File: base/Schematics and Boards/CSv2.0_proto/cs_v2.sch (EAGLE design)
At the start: 80 parts, among them J101 J-JTAG-CORTEX-NEEDLE6LEGS, J301 HIROSE-DF40_44-PIN_CONNECTORS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, J302 HIROSE-DF40_30-PIN_CONNECTORS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, Q201 FK3303010L, Q202 DMG3415UFY4Q-7, Q203 FK3303010L, Q204 FK3303010L, U101 ATSAMD51, U102 AT25SF641-MHB-T, U201 COULOMB-MAX17262, U202 MAX77827BEWC+T, U203 SENSOR-SI7006, U204 LOADSWITCH-MIC94164, U205 LOADSWITCH-MIC94164, Y101 16M, Y102 ABS07-32.768KHZ-9-T

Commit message: Avoided catastrophe from file inconsistencies
Several hours of nightmare-inducing file-fiddling later...
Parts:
- J101: value J-JTAG-CORTEX-NEEDLE6LEGS -> J-JTAG-CORTEX-NEEDLE6-LEGS; device Connectors:J-JTAG-CORTEX-NEEDLE6LEGS -> Connectors:J-JTAG-CORTEX-NEEDLE6-LEGS
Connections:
- removed net N$1: S201.O
- net CC_IN: no longer S201.O
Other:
- moved on the sheet: C201, C203, U201
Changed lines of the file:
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@@
 <part name="JP205" library="Connectors" deviceset="JUMPER-SMT_2_NC_PASTE" device="_NO-SILK" package3d_urn="urn:adsk.eagle:package:39283/1"/>
 <part name="JP204" library="Connectors" deviceset="JUMPER-SMT_2_NC_PASTE" device="_NO-SILK" package3d_urn="urn:adsk.eagle:package:39283/1"/>
-<part name="J101" library="Connectors" deviceset="J-JTAG-CORTEX-NEEDLE6" device="LEGS"/>
+<part name="J101" library="Connectors" deviceset="J-JTAG-CORTEX-NEEDLE6" device="-LEGS"/>
 <part name="R106" library="Resistors" deviceset="R-" device="0402" value="1k">
 <attribute name="PART_NO" value="ERJ-2GEJ102X"/>
@@
 </segment>
 </net>
-<net name="N$1" class="0">
-<segment>
-<pinref part="S201" gate="1" pin="O"/>
-<wire x1="104.14" y1="177.8" x2="109.22" y2="177.8" width="0.1524" layer="91"/>
-</segment>
-</net>
 </nets>
 </sheet>
@@
 should be placed near XTALs</text>
 <text x="121.92" y="193.04" size="3.81" layer="91">Current Monitor</text>
-<text x="165.1" y="182.88" size="1.778" layer="91">Do we lose info about battery
+<text x="165.1" y="177.8" size="1.778" layer="91">Do we lose info about battery
 by not having the input directly
 connected to the battery?</text>
@@
 <attribute name="PART_NO" x="99.06" y="175.26" size="1.778" layer="96" display="off"/>
 </instance>
-<instance part="U201" gate="G$1" x="137.16" y="172.72" smashed="yes">
-<attribute name="NAME" x="127" y="185.42" size="1.778" layer="95"/>
-<attribute name="MP" x="137.16" y="172.72" size="1.778" layer="96" display="off"/>
-<attribute name="PART_NO" x="137.16" y="172.72" size="1.778" layer="96" display="off"/>
-</instance>
-<instance part="C201" gate="G$1" x="111.76" y="172.72" smashed="yes">
-<attribute name="NAME" x="112.776" y="173.355" size="1.778" layer="95"/>
-<attribute name="VALUE" x="112.776" y="168.529" size="1.778" layer="96"/>
-<attribute name="MP" x="111.76" y="172.72" size="1.778" layer="96" display="off"/>
-<attribute name="PART_NO" x="111.76" y="172.72" size="1.778" layer="96" display="off"/>
-</instance>
-<instance part="C203" gate="G$1" x="154.94" y="157.48" smashed="yes">
-<attribute name="NAME" x="155.956" y="158.115" size="1.778" layer="95"/>
-<attribute name="VALUE" x="155.956" y="153.289" size="1.778" layer="96"/>
-<attribute name="MP" x="154.94" y="157.48" size="1.778" layer="96" display="off"/>
-<attribute name="PART_NO" x="154.94" y="157.48" size="1.778" layer="96" display="off"/>
-</instance>
-<instance part="GND217" gate="1" x="154.94" y="147.32" smashed="yes">
-<attribute name="VALUE" x="147.193" y="146.685" size="1.778" layer="96"/>
-</instance>
-<instance part="GND211" gate="1" x="111.76" y="162.56" smashed="yes">
-<attribute name="VALUE" x="109.093" y="159.385" size="1.778" layer="96"/>
-</instance>
-<instance part="GND214" gate="1" x="137.16" y="152.4" smashed="yes">
-<attribute name="VALUE" x="134.493" y="149.225" size="1.778" layer="96"/>
+<instance part="U201" gate="G$1" x="137.16" y="167.64" smashed="yes">
+<attribute name="NAME" x="127" y="180.34" size="1.778" layer="95"/>
+<attribute name="MP" x="137.16" y="167.64" size="1.778" layer="96" display="off"/>
+<attribute name="PART_NO" x="137.16" y="167.64" size="1.778" layer="96" display="off"/>
+</instance>
+<instance part="C201" gate="G$1" x="111.76" y="167.64" smashed="yes">
+<attribute name="NAME" x="112.776" y="168.275" size="1.778" layer="95"/>
+<attribute name="VALUE" x="112.776" y="163.449" size="1.778" layer="96"/>
+<attribute name="MP" x="111.76" y="167.64" size="1.778" layer="96" display="off"/>
+<attribute name="PART_NO" x="111.76" y="167.64" size="1.778" layer="96" display="off"/>
+</instance>
+<instance part="C203" gate="G$1" x="154.94" y="152.4" smashed="yes">
+<attribute name="NAME" x="155.956" y="153.035" size="1.778" layer="95"/>
+<attribute name="VALUE" x="155.956" y="148.209" size="1.778" layer="96"/>
+<attribute name="MP" x="154.94" y="152.4" size="1.778" layer="96" display="off"/>
+<attribute name="PART_NO" x="154.94" y="152.4" size="1.778" layer="96" display="off"/>
+</instance>
+<instance part="GND217" gate="1" x="154.94" y="142.24" smashed="yes">
+<attribute name="VALUE" x="147.193" y="141.605" size="1.778" layer="96"/>
+</instance>
+<instance part="GND211" gate="1" x="111.76" y="157.48" smashed="yes">
+<attribute name="VALUE" x="109.093" y="154.305" size="1.778" layer="96"/>
+</instance>
+<instance part="GND214" gate="1" x="137.16" y="147.32" smashed="yes">
+<attribute name="VALUE" x="134.493" y="144.145" size="1.778" layer="96"/>
 </instance>
 <instance part="C202" gate="G$1" x="149.86" y="101.6" smashed="yes">
@@
 <pinref part="C201" gate="G$1" pin="2"/>
 <pinref part="GND211" gate="1" pin="GND"/>
-<wire x1="111.76" y1="167.64" x2="111.76" y2="165.1" width="0.1524" layer="91"/>
+<wire x1="111.76" y1="162.56" x2="111.76" y2="160.02" width="0.1524" layer="91"/>
 </segment>
 <segment>
 <pinref part="C203" gate="G$1" pin="2"/>
 <pinref part="GND217" gate="1" pin="GND"/>
-<wire x1="154.94" y1="152.4" x2="154.94" y2="149.86" width="0.1524" layer="91"/>
+<wire x1="154.94" y1="147.32" x2="154.94" y2="144.78" width="0.1524" layer="91"/>
 </segment>
 <segment>
 <pinref part="GND214" gate="1" pin="GND"/>
 <pinref part="U201" gate="G$1" pin="GND"/>
-<wire x1="137.16" y1="154.94" x2="137.16" y2="157.48" width="0.1524" layer="91"/>
+<wire x1="137.16" y1="149.86" x2="137.16" y2="152.4" width="0.1524" layer="91"/>
 </segment>
 <segment>
@@
 <segment>
 <pinref part="U201" gate="G$1" pin="REG"/>
-<wire x1="149.86" y1="162.56" x2="154.94" y2="162.56" width="0.1524" layer="91"/>
+<wire x1="149.86" y1="157.48" x2="154.94" y2="157.48" width="0.1524" layer="91"/>
 <pinref part="C203" gate="G$1" pin="1"/>
 </segment>
@@
 <pinref part="U201" gate="G$1" pin="BATT"/>
 <pinref part="C201" gate="G$1" pin="1"/>
-<wire x1="111.76" y1="177.8" x2="121.92" y2="177.8" width="0.1524" layer="91"/>
-<wire x1="121.92" y1="177.8" x2="124.46" y2="177.8" width="0.1524" layer="91"/>
+<wire x1="111.76" y1="172.72" x2="121.92" y2="172.72" width="0.1524" layer="91"/>
+<wire x1="121.92" y1="172.72" x2="124.46" y2="172.72" width="0.1524" layer="91"/>
 <pinref part="U201" gate="G$1" pin="TH"/>
-<wire x1="124.46" y1="162.56" x2="121.92" y2="162.56" width="0.1524" layer="91"/>
-<wire x1="121.92" y1="162.56" x2="121.92" y2="177.8" width="0.1524" layer="91"/>
-<junction x="121.92" y="177.8"/>
-<junction x="111.76" y="177.8"/>
-<pinref part="S201" gate="1" pin="O"/>
-<wire x1="111.76" y1="177.8" x2="104.14" y2="177.8" width="0.1524" layer="91"/>
+<wire x1="124.46" y1="157.48" x2="121.92" y2="157.48" width="0.1524" layer="91"/>
+<wire x1="121.92" y1="157.48" x2="121.92" y2="172.72" width="0.1524" layer="91"/>
+<junction x="121.92" y="172.72"/>
 </segment>
 </net>
@@
 <junction x="182.88" y="121.92"/>
 <pinref part="U201" gate="G$1" pin="SYS"/>
-<wire x1="149.86" y1="177.8" x2="182.88" y2="177.8" width="0.1524" layer="91"/>
-<wire x1="182.88" y1="177.8" x2="182.88" y2="121.92" width="0.1524" layer="91"/>
+<wire x1="149.86" y1="172.72" x2="182.88" y2="172.72" width="0.1524" layer="91"/>
+<wire x1="182.88" y1="172.72" x2="182.88" y2="121.92" width="0.1524" layer="91"/>
 </segment>
 </net>
@@
 <segment>
 <pinref part="U201" gate="G$1" pin="SDA"/>
-<wire x1="149.86" y1="170.18" x2="152.4" y2="170.18" width="0.1524" layer="91"/>
-<label x="152.4" y="170.18" size="1.27" layer="95" xref="yes"/>
+<wire x1="149.86" y1="165.1" x2="152.4" y2="165.1" width="0.1524" layer="91"/>
+<label x="152.4" y="165.1" size="1.27" layer="95" xref="yes"/>
 </segment>
 <segment>
@@
 <segment>
 <pinref part="U201" gate="G$1" pin="SCL"/>
-<wire x1="149.86" y1="167.64" x2="152.4" y2="167.64" width="0.1524" layer="91"/>
-<label x="152.4" y="167.64" size="1.27" layer="95" xref="yes"/>
-</segment>
-<segment>
+<wire x1="149.86" y1="162.56" x2="152.4" y2="162.56" width="0.1524" layer="91"/>
+<label x="152.4" y="162.56" size="1.27" layer="95" xref="yes"/>
+</segment>
+<segment>

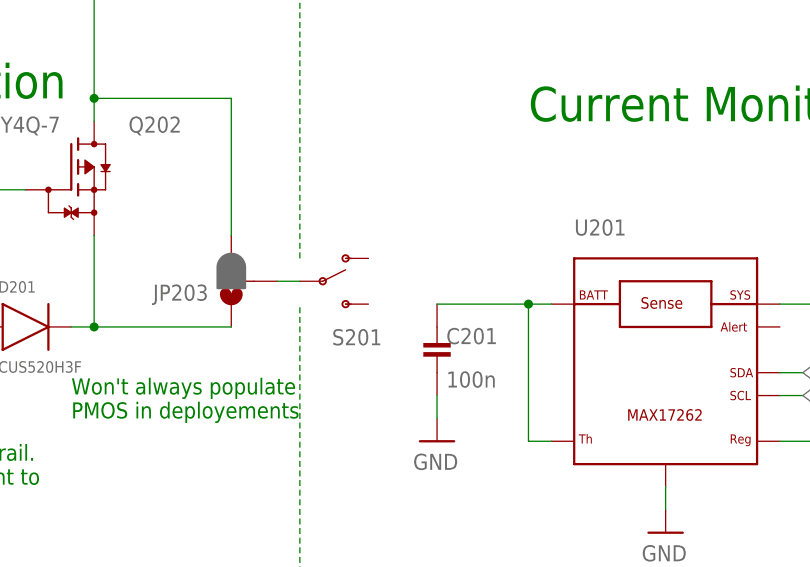
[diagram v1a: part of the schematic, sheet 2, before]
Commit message: A few small manual routes
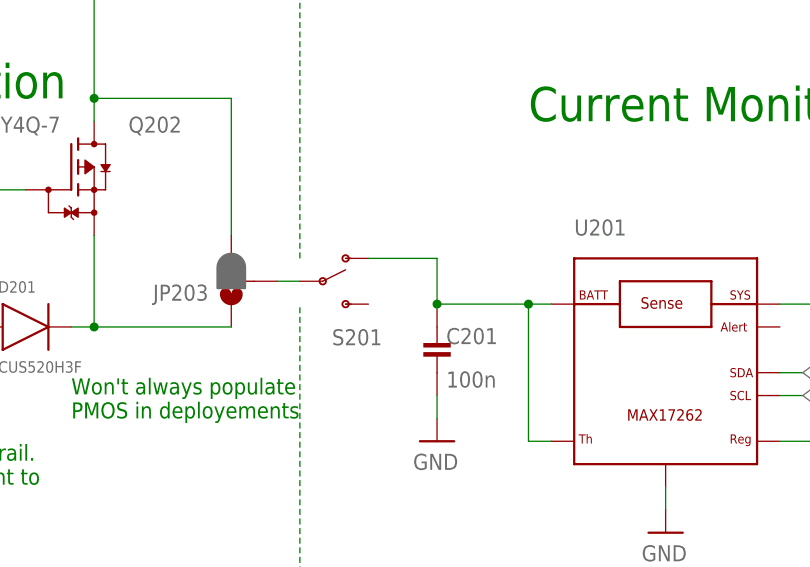
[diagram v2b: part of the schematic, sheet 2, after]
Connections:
- net CC_IN: now also S201.O
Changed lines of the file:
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@@
 <wire x1="121.92" y1="157.48" x2="121.92" y2="172.72" width="0.1524" layer="91"/>
 <junction x="121.92" y="172.72"/>
+<pinref part="S201" gate="1" pin="O"/>
+<wire x1="104.14" y1="177.8" x2="111.76" y2="177.8" width="0.1524" layer="91"/>
+<wire x1="111.76" y1="177.8" x2="111.76" y2="172.72" width="0.1524" layer="91"/>
+<junction x="111.76" y="172.72"/>
 </segment>
 </net>

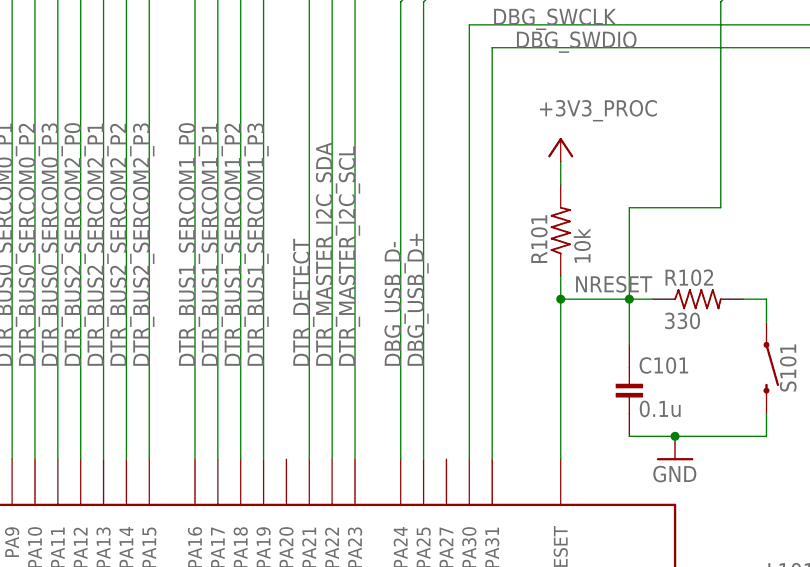
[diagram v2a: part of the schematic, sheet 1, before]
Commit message: Hand route a handful of signals to non-connector parts
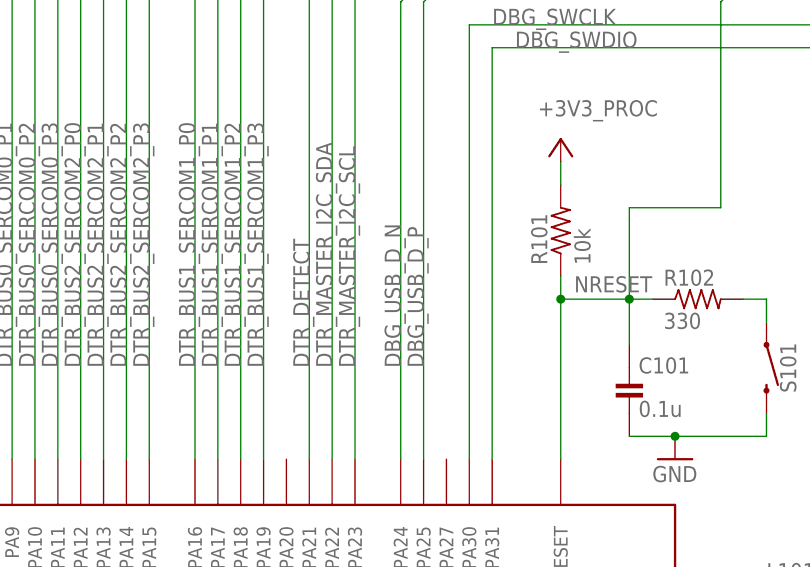
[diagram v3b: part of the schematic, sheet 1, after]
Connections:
- net DBG_USB_D+ renamed DBG_USB_D_P
- net DBG_USB_D- renamed DBG_USB_D_N
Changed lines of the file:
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@@
 <class number="1" name="power_3v3" width="0.254" drill="0">
+</class>
+<class number="2" name="differential" width="0" drill="0">
 </class>
 <class number="5" name="10_mil" width="0.254" drill="0">
@@
 <label x="137.16" y="200.66" size="1.778" layer="95" rot="R90"/>
 <wire x1="137.16" y1="251.46" x2="139.7" y2="254" width="0.1524" layer="91"/>
-</segment>
-</net>
-<net name="DBG_USB_D-" class="0">
-<segment>
-<pinref part="U101" gate="G$1" pin="PA24"/>
-<wire x1="165.1" y1="190.5" x2="165.1" y2="241.3" width="0.1524" layer="91"/>
-<label x="165.1" y="200.66" size="1.778" layer="95" rot="R90"/>
-<wire x1="165.1" y1="241.3" x2="167.64" y2="243.84" width="0.1524" layer="91"/>
-</segment>
-</net>
-<net name="DBG_USB_D+" class="0">
-<segment>
-<pinref part="U101" gate="G$1" pin="PA25"/>
-<wire x1="167.64" y1="190.5" x2="167.64" y2="241.3" width="0.1524" layer="91"/>
-<label x="167.64" y="200.66" size="1.778" layer="95" rot="R90"/>
-<wire x1="167.64" y1="241.3" x2="170.18" y2="243.84" width="0.1524" layer="91"/>
 </segment>
 </net>
@@
 </segment>
 </net>
+<net name="DBG_USB_D_N" class="2">
+<segment>
+<pinref part="U101" gate="G$1" pin="PA24"/>
+<wire x1="165.1" y1="190.5" x2="165.1" y2="241.3" width="0.1524" layer="91"/>
+<label x="165.1" y="200.66" size="1.778" layer="95" rot="R90"/>
+<wire x1="165.1" y1="241.3" x2="167.64" y2="243.84" width="0.1524" layer="91"/>
+</segment>
+</net>
+<net name="DBG_USB_D_P" class="2">
+<segment>
+<pinref part="U101" gate="G$1" pin="PA25"/>
+<wire x1="167.64" y1="190.5" x2="167.64" y2="241.3" width="0.1524" layer="91"/>
+<label x="167.64" y="200.66" size="1.778" layer="95" rot="R90"/>
+<wire x1="167.64" y1="241.3" x2="170.18" y2="243.84" width="0.1524" layer="91"/>
+</segment>
+</net>
 </nets>
 </sheet>
@@
 </segment>
 </net>
-<net name="DBG_USB_D-" class="0">
+<net name="DBG_USB_D_N" class="2">
 <segment>
 <wire x1="281.94" y1="218.44" x2="284.48" y2="215.9" width="0.1524" layer="91"/>
@@
 </segment>
 </net>
-<net name="DBG_USB_D+" class="0">
+<net name="DBG_USB_D_P" class="2">
 <segment>
 <wire x1="284.48" y1="218.44" x2="287.02" y2="215.9" width="0.1524" layer="91"/>

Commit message: Changed 1 part number. Included in BOM of previous commit
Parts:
- R101: PART_NO P10KJCT-ND -> ERJ-2GEJ103X
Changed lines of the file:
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@@
 <part name="GND7" library="Supplies" deviceset="GND" device=""/>
 <part name="R101" library="Resistors" deviceset="R-" device="0402" value="10k">
-<attribute name="PART_NO" value="P10KJCT-ND "/>
+<attribute name="PART_NO" value="ERJ-2GEJ103X"/>
 </part>
 <part name="R102" library="Resistors" deviceset="R-" device="0402" value="330">
